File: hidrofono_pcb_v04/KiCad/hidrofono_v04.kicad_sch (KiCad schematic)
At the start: 12 parts, among them J1 1 PIEZO_IN / 2 PIEZO_GND, J2 CABLE, J3 GND_AGUA, Q1 2SK209-Y

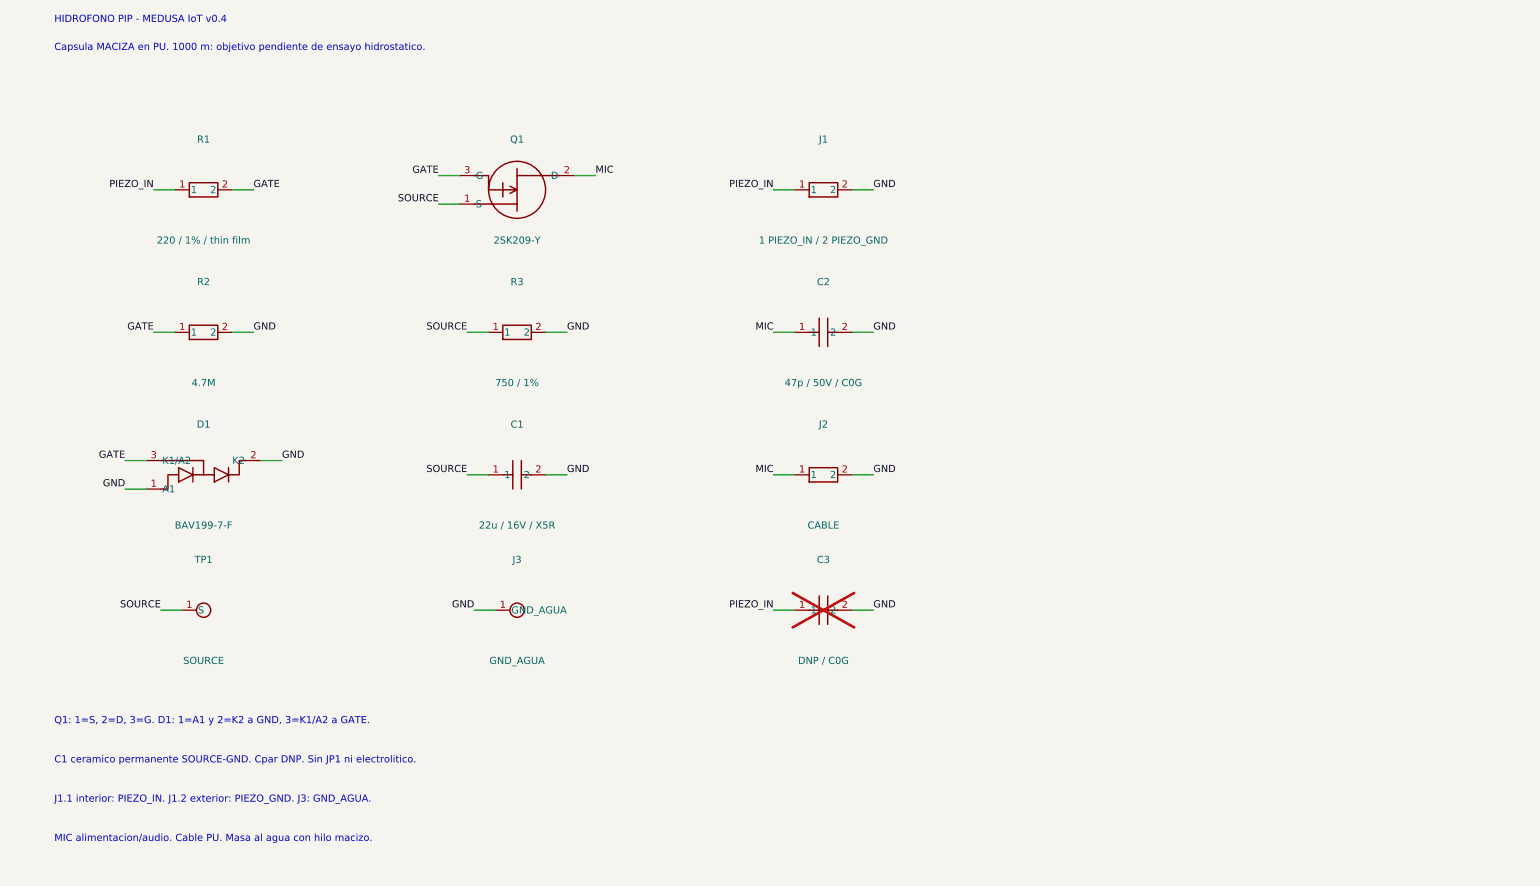
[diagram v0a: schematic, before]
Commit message: Redraw v0.4 schematic with wires and add capsule connection illustration
Schematic regenerated as a wired circuit with clearer symbols, keeping
references, UUIDs, footprints, fields and net names; KiCad 7 netlist is
pin-for-pin identical to v0.4, so the PCB and Gerbers are unchanged.
Adds schematic PDF, a connection illustration (piezo, cable, water
ground, test point, anchors, side section) and notes that the J1
silkscreen labels are stacked in reverse pad order.

Co-Authored-By: Claude Opus 5.5 <noreply@anthropic.com>
Claude-Session: https://claude.ai/code/session_01MFuLsVxzc9PK6N6Wwu2ciG
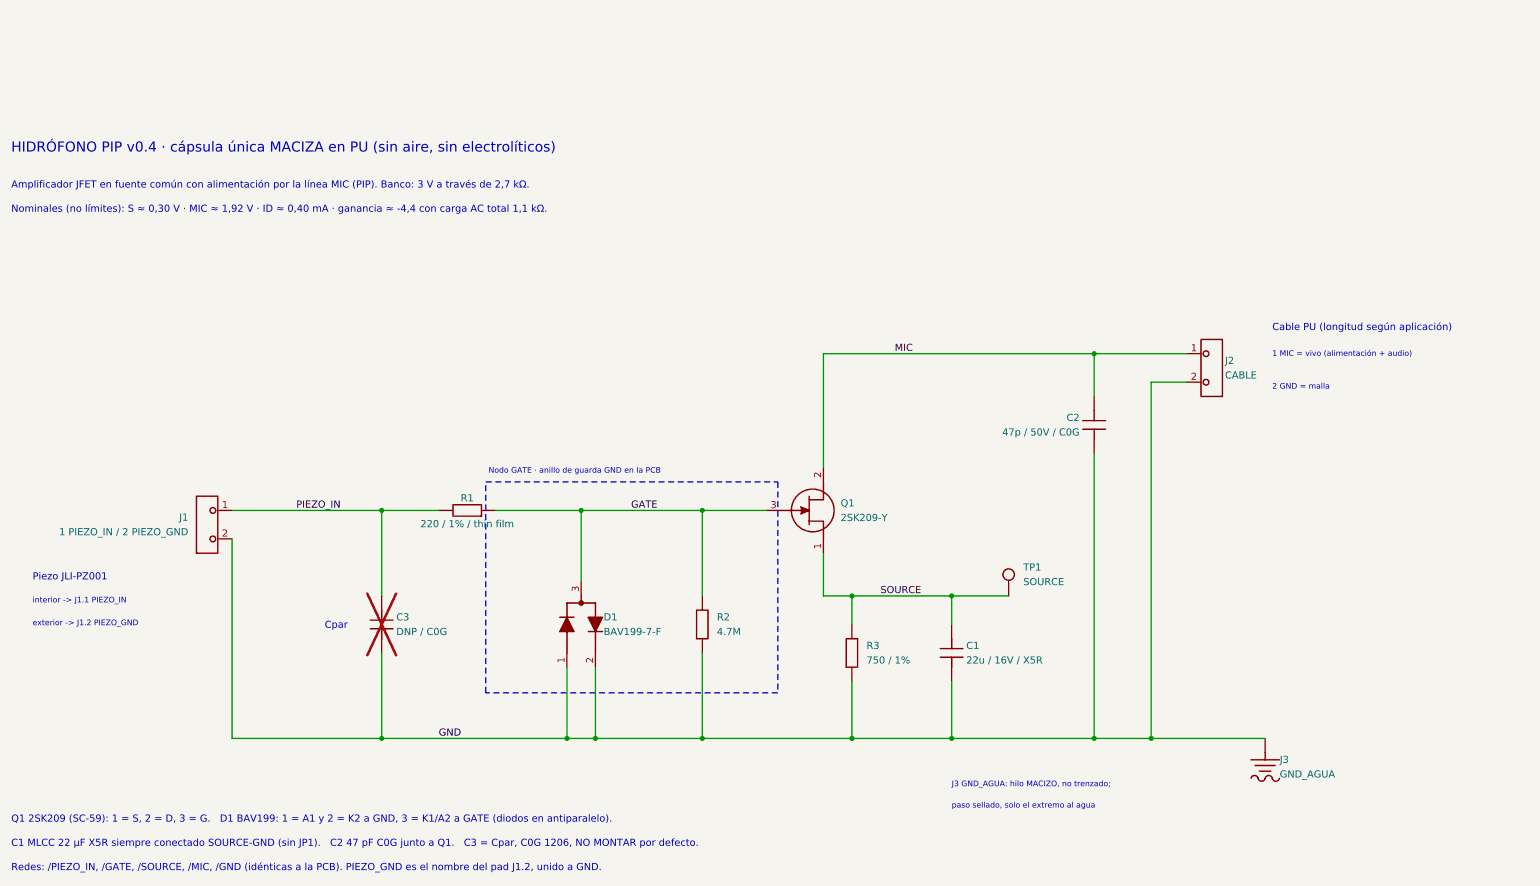
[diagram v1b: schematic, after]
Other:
- note added: "1 MIC = vivo (alimentación + audio)"
- note added: "2 GND = malla"
- note added: "Amplificador JFET en fuente común con alimentación por la línea MIC (PIP). Banco: 3 V a través de 2,7 kΩ."
- note added: "C1 MLCC 22 µF X5R siempre conectado SOURCE-GND (sin JP1). C2 47 pF C0G junto a Q1. C3 = Cpar, C0G 1206, NO MONTAR por defecto."
- note added: "Cable PU (longitud según aplicación)"
- note added: "Cpar"
- note added: "HIDRÓFONO PIP v0.4 · cápsula única MACIZA en PU (sin aire, sin electrolíticos)"
- note added: "J3 GND_AGUA: hilo MACIZO, no trenzado;"
- note added: "Nodo GATE · anillo de guarda GND en la PCB"
- note added: "Nominales (no límites): S ≈ 0,30 V · MIC ≈ 1,92 V · ID ≈ 0,40 mA · ganancia ≈ -4,4 con carga AC total 1,1 kΩ."
- note added: "Piezo JLI-PZ001"
- note added: "Q1 2SK209 (SC-59): 1 = S, 2 = D, 3 = G. D1 BAV199: 1 = A1 y 2 = K2 a GND, 3 = K1/A2 a GATE (diodos en antiparalelo)."
- note added: "Redes: /PIEZO_IN, /GATE, /SOURCE, /MIC, /GND (idénticas a la PCB). PIEZO_GND es el nombre del pad J1.2, unido a GND."
- note added: "exterior -> J1.2 PIEZO_GND"
- note added: "interior -> J1.1 PIEZO_IN"
- note added: "paso sellado, solo el extremo al agua"
- note removed: "C1 ceramico permanente SOURCE-GND. Cpar DNP. Sin JP1 ni electrolitico."
- note removed: "Capsula MACIZA en PU. 1000 m: objetivo pendiente de ensayo hidrostatico."
- note removed: "HIDROFONO PIP - MEDUSA IoT v0.4"
- note removed: "J1.1 interior: PIEZO_IN. J1.2 exterior: PIEZO_GND. J3: GND_AGUA."
- note removed: "MIC alimentacion/audio. Cable PU. Masa al agua con hilo macizo."
- note removed: "Q1: 1=S, 2=D, 3=G. D1: 1=A1 y 2=K2 a GND, 3=K1/A2 a GATE."
- moved on the sheet: J1, J2
